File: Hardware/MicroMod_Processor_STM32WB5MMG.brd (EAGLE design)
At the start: 160 x 100 mm, 0 parts

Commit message: Nearing layout completion.
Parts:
- added C1, C2: 0.1uF, SparkFun-Capacitors:0402-TIGHT
- added D1: 120mA/40V/370mV, SparkFun-DiscreteSemi:SOD-523
- added D2: BLUE, SparkFun-LED:LED-0603
- added FD1, FD2, FD3, FD4: FIDUCIALUFIDUCIAL, SparkFun-Aesthetics:FIDUCIAL-MICRO
- added FRAME2: FRAME-LETTER, SparkFun-Aesthetics:CREATIVE_COMMONS
- added J1: MICROMOD-2222, SparkFun-MicroMod:M.2-CARD-E-22
- added LOGO1: FOUR_LAYER_WARNING, SparkFun-Aesthetics:FOUR_LAYER_WARNING
- added LOGO2: OSHW-LOGOMINI, SparkFun-Aesthetics:OSHW-LOGO-MINI
- added LOGO3: SFE_LOGO_NAME_FLAME.1_INCH, SparkFun-Aesthetics:SFE_LOGO_NAME_FLAME_.1
- added LOGO4: SPECIAL_INSTRUCTIONS-ORDERING, SparkFun-Aesthetics:ORDERING_INSTRUCTIONS
- added Q1: 20V/4.2A/52mΩ/1.4W, SparkFun-DiscreteSemi:SOT23-3
- added R1, R2: 100k, SparkFun-Resistors:0402-TIGHT
- added R3: 2.2k, SparkFun-Resistors:0402-TIGHT
- added U$1: (no value), SparkFun-MicroMod:MICROMOD_MI_LOGO_.35
- added U$2: (no value), SparkFun-MicroMod:MICROMOD_LOGO_.3
- added U$3: (no value), SparkFun-Aesthetics:SFE_LOGO_FLAME_.1
- added U1: STM32WB5MMG, stm32wb5mmg:SIP-LGA86
- added U2: W25QXX128MBIT-6X5, SparkFun-IC-Memory:WSON-8-6X5
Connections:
- new net !BOOT!: J1.11, Q1.1, R2.1
- new net !RESET!: C1.1, J1.6, U1.10
- new net 3.3V: C2.1, D1.A, J1.2, J1.74, Q1.2, R2.2, U1.17, U1.32, U1.4, U1.6, U2.8
- new net A0: J1.34, U1.8
- new net A1: J1.38, U1.7
- new net AUD_BCLK: J1.50, U1.50
- new net AUD_FSYNC: J1.52, U1.11
- new net AUD_I2S_IN: J1.54, U1.19
- new net AUD_I2S_OUT: J1.56, U1.38
- new net AUD_MCLK: J1.58, U1.14
- new net BATT_VIN: J1.49, U1.49
- new net BOOT0: Q1.3, R1.2, U1.13
- new net GND: C1.2, C2.2, D2.C, J1.1, J1.33, J1.36, J1.39, J1.45, J1.7, J1.75, J1.GND1, J1.GND2, J1.GND3, R1.1, U1.16, U1.31, U1.5, U1.57, U1.58, U1.59, U1.60, U1.84, U1.86, U2.4
- new net I2C1_INT: J1.16, U1.2
- new net I2C1_SCL: J1.14, U1.39
- new net I2C1_SDA: J1.12, U1.18
- new net I2C3_SCL: J1.53, U1.35
- new net I2C3_SDA: J1.51, U1.37
- new net LPUART_RX/DEV_TX: J1.20, U1.12
- new net LPUART_TX/DEV_RX: J1.22, U1.9
- new net N$1: D2.A, R3.1
- new net PA0/G5: J1.73, U1.3
- new net PC11/G1: J1.42, U1.23
- new net PC13/G2: J1.44, U1.40
- new net PD8/G3: J1.46, U1.75
- new net PE3/G4: J1.48, U1.72
- new net PE4/G0: J1.40, U1.42
- new net PH0/G7: J1.69, U1.61
- new net PH1/G6: J1.71, U1.62
- new net PWM0: J1.32, U1.63
- new net PWM1: J1.47, U1.76
- new net QSPI_!CS!: U1.70, U2.1
- new net QSPI_CLK: U1.56, U2.6
- new net QSPI_IO0: U1.73, U2.5
- new net QSPI_IO1: U1.80, U2.2
- new net QSPI_IO2: U1.81, U2.3
- new net QSPI_IO3: U1.67, U2.7
- new net SPI_!CS!: J1.55, U1.55
- new net SPI_PICO: J1.59, U1.52
- new net SPI_POCI: J1.61, U1.53
- new net SPI_SCK: J1.57, U1.54
- new net STAT: R3.2, U1.1
- new net SWDCK: J1.21, U1.26
- new net SWDIO: J1.23, U1.25
- new net TIM1_BKIN: J1.10, U1.41
- new net TIM1_ETR: J1.18, U1.79
- new net UART_CTS: J1.15, U1.20
- new net UART_RTS_DE: J1.13, U1.21
- new net UART_RX/DEV_TX: J1.19, U1.28
- new net UART_TX/DEV_RX: J1.17, U1.51
- new net USB_N: J1.5, U1.30
- new net USB_P: J1.3, U1.29
- new net V_BATT: D1.C, J1.72, U1.15
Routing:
- net A0: track 0.00 -> 33.5 mm, vias 0 -> 3
- net !RESET!: track 0.00 -> 31.8 mm, vias 0 -> 2
- net I2C1_INT: track 0.00 -> 31.5 mm, vias 0 -> 3
- net A1: track 0.00 -> 31.3 mm, vias 0 -> 3
- net TIM1_ETR: track 0.00 -> 27.6 mm, vias 0 -> 3
- net LPUART_TX/DEV_RX: track 0.00 -> 25.3 mm, vias 0 -> 2
- net TIM1_BKIN: track 0.00 -> 24.8 mm, vias 0 -> 2
- net PC13/G2: track 0.00 -> 24.7 mm, vias 0 -> 3
- net I2C1_SCL: track 0.00 -> 24.6 mm, vias 0 -> 2
- net LPUART_RX/DEV_TX: track 0.00 -> 24.1 mm, vias 0 -> 2
- net I2C1_SDA: track 0.00 -> 24.0 mm, vias 0 -> 1
- net AUD_I2S_OUT: track 0.00 -> 23.6 mm, vias 0 -> 2
- net QSPI_CLK: track 0.00 -> 23.4 mm, vias 0 -> 2
- net PD8/G3: track 0.00 -> 23.3 mm, vias 0 -> 4
- net QSPI_IO3: track 0.00 -> 22.9 mm, vias 0 -> 2
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- added copper zone on layer 15, net 3.3V
- added copper zone on layer 1, net GND
- added copper zone on layer 16, net GND
- added copper zone on layer 2, net GND
- added copper zone on layer 15, net GND1
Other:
- board size 160 x 100 mm -> 22 x 22 mm
- board text added: "Alex Brudner"

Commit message: Layout complete.
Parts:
- added TP1, TP2, TP3, TP4, TP5, TP6, TP7, TP8: TEST-POINT3, SparkFun-Connectors:PAD.03X.03
- added U$4, U$5: (no value), output:STM32WB5MMG0
- added U$6: (no value), SparkFun-Aesthetics:SFE_LOGO_FLAME_STOP_.1
- moved U$3 49.4 mm to (10.8, 12.6)
- moved U$2 47.7 mm to (14.6, 10.2), flipped to the bottom, turned to 90 degrees
- moved U$1 47.1 mm to (17.9, 7.15)
- moved LOGO3 34.3 mm to (18.1, 10.6), flipped to the bottom, turned to 90 degrees
- moved LOGO2 31.6 mm to (16.0, 17.0)
- moved FRAME2 21.2 mm to (52.1, -18.6)
- moved LOGO1 21.2 mm to (28.4, 30.4)
- moved LOGO4 21.2 mm to (25.7, 42.5)
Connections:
- net BOOT0: now also TP1.1
- net QSPI_!CS!: now also TP4.1
- net QSPI_CLK: now also TP3.1
- net QSPI_IO0: now also TP5.1
- net QSPI_IO1: now also TP6.1
- net QSPI_IO2: now also TP7.1
- net QSPI_IO3: now also TP8.1
- net STAT: now also TP2.1
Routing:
- net PH0/G7: track 0.00 -> 26.1 mm, vias 1 -> 3
- net PH1/G6: track 0.00 -> 25.5 mm, vias 1 -> 3
- net QSPI_IO2: track 10.2 -> 14.0 mm
- net STAT: track 18.2 -> 20.3 mm
- net PD8/G3: track 23.3 -> 25.3 mm
- net QSPI_!CS!: track 8.92 -> 10.7 mm
- net GND: track 1.32 -> 0.00 mm, vias 35 -> 41
- net QSPI_IO1: track 11.2 -> 12.1 mm
- net QSPI_IO3: track 22.9 -> 23.8 mm
- net BOOT0: track 16.2 -> 17.0 mm
- net AUD_MCLK: track 14.9 -> 15.6 mm
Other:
- board text added: "1"
- board text added: "2"
- board text added: "3"
- board text added: "4"
- board text added: "Beveled Edge"
- board text added: "Board Thickness is 0.8mm"
- board text added: "ENIG Finish"
- board text added: "v01"

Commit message: Last update for protos.
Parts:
- added U$7: (no value), output:STAT0
- moved TP3 13.3 mm to (5.08, 15.2)
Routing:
- net QSPI_CLK: track 23.7 -> 22.7 mm
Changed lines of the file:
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@@
 <layer number="29" name="tStop" color="7" fill="3" visible="yes" active="yes"/>
 <layer number="30" name="bStop" color="7" fill="6" visible="yes" active="yes"/>
-<layer number="31" name="tCream" color="7" fill="4" visible="no" active="yes"/>
+<layer number="31" name="tCream" color="7" fill="4" visible="yes" active="yes"/>
 <layer number="32" name="bCream" color="7" fill="5" visible="no" active="yes"/>
 <layer number="33" name="tFinish" color="6" fill="3" visible="no" active="yes"/>
@@
 <elements>
 <element name="J1" library="SparkFun-MicroMod" package="M.2-CARD-E-22" value="MICROMOD-2222" x="11" y="0" smashed="yes"/>
-<element name="U1" library="stm32wb5mmg" package="SIP-LGA86" value="STM32WB5MMG" x="4.95" y="16.1" locked="yes" smashed="yes">
-<attribute name="PROD_ID" value="IC-17415" x="4.92" y="16.13" locked="yes" size="1.778" layer="27" display="off"/>
+<element name="U1" library="stm32wb5mmg" package="SIP-LGA86" value="STM32WB5MMG" x="4.95" y="16.1" smashed="yes">
+<attribute name="PROD_ID" value="IC-17415" x="4.92" y="16.13" size="1.778" layer="27" display="off"/>
 </element>
 <element name="C1" library="SparkFun-Capacitors" package="0402-TIGHT" value="0.1uF" x="1.55" y="7.7" smashed="yes">
@@
 <element name="U$5" library="output" package="STM32WB5MMG0" value="" x="16.1" y="10.7" smashed="yes" rot="MR90"/>
 <element name="U$6" library="SparkFun-Aesthetics" package="SFE_LOGO_FLAME_STOP_.1" value="" x="19.25" y="19.8" smashed="yes" rot="MR0"/>
-<element name="TP3" library="SparkFun-Connectors" package="PAD.03X.03" value="TEST-POINT3" x="17.78" y="11.43" smashed="yes" rot="MR0"/>
+<element name="TP3" library="SparkFun-Connectors" package="PAD.03X.03" value="TEST-POINT3" x="5.08" y="15.24" smashed="yes" rot="MR0"/>
 <element name="TP4" library="SparkFun-Connectors" package="PAD.03X.03" value="TEST-POINT3" x="13.97" y="11.43" smashed="yes" rot="MR0"/>
 <element name="TP5" library="SparkFun-Connectors" package="PAD.03X.03" value="TEST-POINT3" x="20.32" y="11.43" smashed="yes" rot="MR0"/>
@@
 <element name="TP1" library="SparkFun-Connectors" package="PAD.03X.03" value="TEST-POINT3" x="11.43" y="10.16" smashed="yes" rot="MR0"/>
 <element name="TP2" library="SparkFun-Connectors" package="PAD.03X.03" value="TEST-POINT3" x="20.32" y="16.51" smashed="yes" rot="MR0"/>
+<element name="U$7" library="output" package="STAT0" value="" x="19.8" y="18.4" smashed="yes"/>
 </elements>
 <signals>
@@
 <wire x1="17.8" y1="12.4" x2="12.25" y2="12.4" width="0.15" layer="16"/>
 <wire x1="12.1" y1="12.25" x2="12.25" y2="12.4" width="0.15" layer="16"/>
-<wire x1="19.45" y1="10.75" x2="18.3" y2="11.9" width="0.15" layer="16"/>
-<wire x1="18.3" y1="11.9" x2="17.8" y2="12.4" width="0.15" layer="16"/>
+<wire x1="19.45" y1="10.75" x2="17.8" y2="12.4" width="0.15" layer="16"/>
 <wire x1="7.75" y1="12.25" x2="12.1" y2="12.25" width="0.15" layer="16"/>
 <wire x1="7.75" y1="12.25" x2="6.8" y2="13.2" width="0.15" layer="16"/>
-<wire x1="6.8" y1="13.2" x2="6.8" y2="13.4" width="0.15" layer="16"/>
-<wire x1="6.8" y1="13.4" x2="6.55" y2="13.65" width="0.15" layer="16"/>
-<wire x1="6.55" y1="13.65" x2="6.15" y2="13.65" width="0.15" layer="16"/>
-<wire x1="6.15" y1="13.65" x2="4.05" y2="15.75" width="0.15" layer="16"/>
-<wire x1="4.05" y1="17.65" x2="4.05" y2="15.75" width="0.15" layer="16"/>
-<wire x1="4.05" y1="17.65" x2="4" y2="17.7" width="0.15" layer="16"/>
 <contactref element="TP3" pad="1"/>
-<wire x1="17.78" y1="11.43" x2="17.83" y2="11.43" width="0.15" layer="16"/>
-<wire x1="17.83" y1="11.43" x2="18.3" y2="11.9" width="0.15" layer="16"/>
+<wire x1="6.8" y1="13.52" x2="5.08" y2="15.24" width="0.15" layer="16"/>
+<wire x1="6.8" y1="13.2" x2="6.8" y2="13.52" width="0.15" layer="16"/>
+<wire x1="4.0036" y1="16.96718125" x2="4" y2="16.97078125" width="0.15" layer="16"/>
+<wire x1="4" y1="16.97078125" x2="4" y2="17.7" width="0.15" layer="16"/>
+<wire x1="5.08" y1="15.24" x2="4.0036" y2="16.3164" width="0.15" layer="16"/>
+<wire x1="4.0036" y1="16.3164" x2="4.0036" y2="16.96718125" width="0.15" layer="16"/>
 </signal>
 <signal name="QSPI_!CS!">

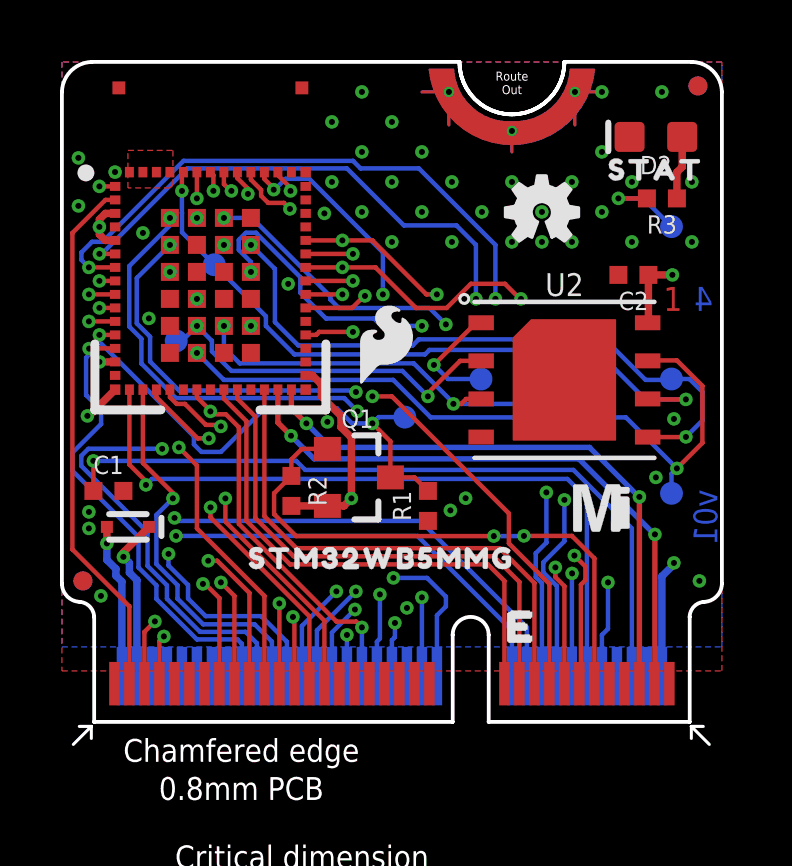
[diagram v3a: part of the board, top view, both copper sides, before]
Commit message: Updates from Design Review v01
Fix footprint.
Reposition bottom silk
Removed extraneous vias.
Renamed some nets to match micromod connector.
Rerouted some traces.
Added ground vias near fast switching vias.
Moved traces to expand ground plane.
Removed all but BOOT0 test point with Chris' approval.
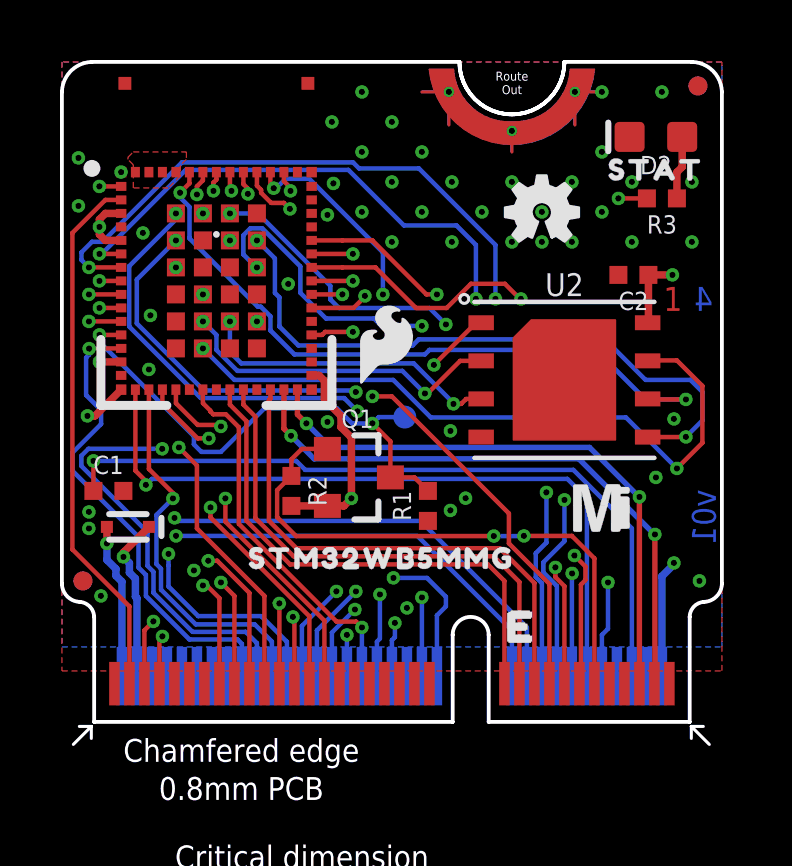
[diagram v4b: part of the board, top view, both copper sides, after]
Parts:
- removed TP2, TP3, TP4, TP5, TP6, TP7, TP8: TEST-POINT3, SparkFun-Connectors:PAD.03X.03
- moved U$5 15.1 mm to (4.85, 20.8), turned to 0 degrees
- moved LOGO3 2.89 mm to (15.6, 11.9), turned to 0 degrees
- moved U$2 1.28 mm to (15.6, 9.35), turned to 0 degrees
- moved U1 0.25 mm to (5.15, 16.2)
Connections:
- net I2C3_SCL renamed I2C3_SCL1
- net I2C3_SDA renamed I2C3_SDA1
- net LPUART_RX/DEV_TX renamed LP_RX2/DEV_TX2
- net LPUART_TX/DEV_RX renamed LP_TX2/DEV_RX2
- net UART_RX/DEV_TX renamed RX1/DEV_TX1
- net UART_TX/DEV_RX renamed TX1/DEV_RX1
- net QSPI_!CS!: no longer TP4.1
- net QSPI_CLK: no longer TP3.1
- net QSPI_IO0: no longer TP5.1
- net QSPI_IO1: no longer TP6.1
- net QSPI_IO2: no longer TP7.1
- net QSPI_IO3: no longer TP8.1
- net STAT: no longer TP2.1
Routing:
- net QSPI_IO2: track 14.0 -> 10.2 mm
- net STAT: track 20.3 -> 18.0 mm
- net QSPI_!CS!: track 10.7 -> 8.78 mm
- net QSPI_IO1: track 12.1 -> 11.0 mm
- net QSPI_IO3: track 23.8 -> 22.7 mm
- net 3.3V: track 21.5 -> 22.1 mm
- net PE4/G0: track 20.4 -> 20.2 mm, vias 3 -> 2
- net PC13/G2: track 24.9 -> 24.7 mm, vias 3 -> 2
- net PC11/G1: track 12.5 -> 12.4 mm, vias 2 -> 1

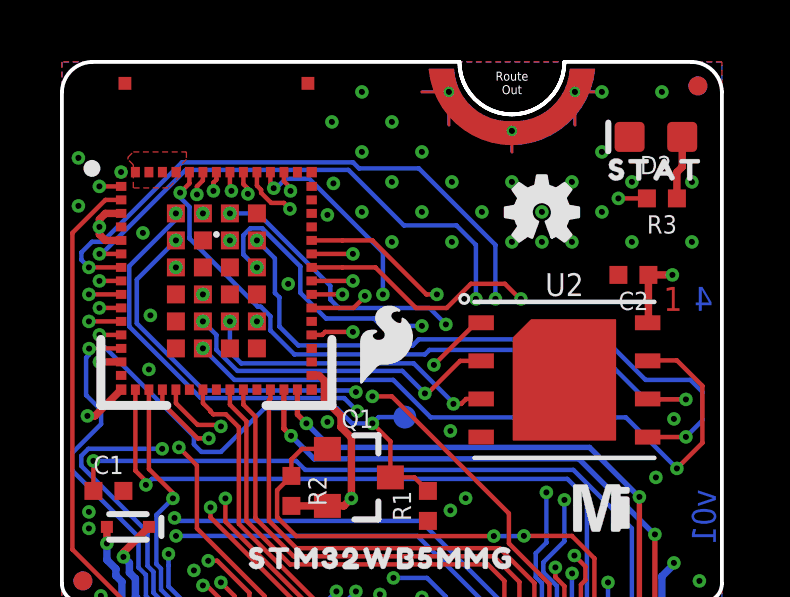
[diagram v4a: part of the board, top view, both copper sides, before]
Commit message: Protos commit
Schematic - Revector all fonts
Board - Straighten one trace.
Panel - Panelize and CAM.
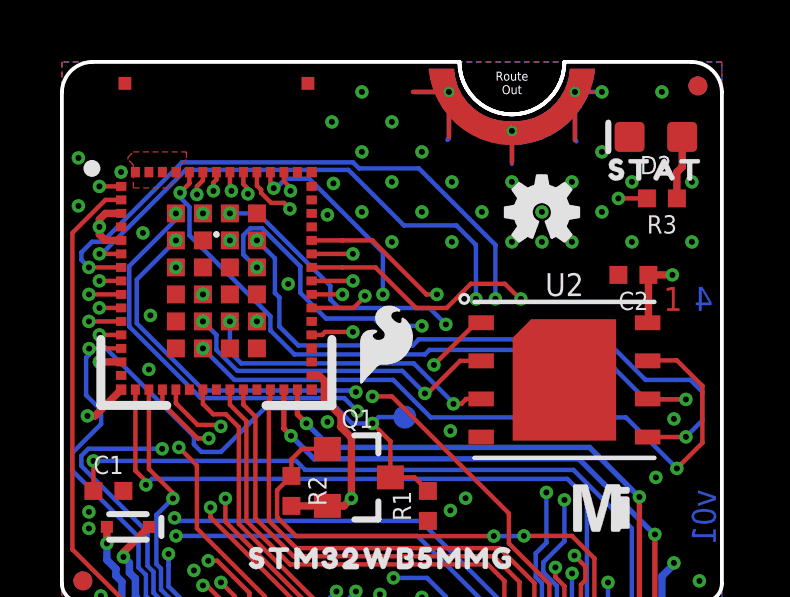
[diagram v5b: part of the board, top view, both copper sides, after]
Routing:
- net GND: track 0.00 -> 11.8 mm
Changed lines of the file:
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@@
 <via x="12.95" y="9.7" extent="1-16" drill="0.2"/>
 <via x="2.9" y="11.75" extent="1-16" drill="0.2"/>
+<wire x1="12.9" y1="21" x2="12.9" y2="19.5" width="0.15" layer="1"/>
+<wire x1="12.9" y1="21" x2="11.7" y2="21" width="0.15" layer="1"/>
+<wire x1="15" y1="19.7" x2="15" y2="18.65" width="0.15" layer="1"/>
+<wire x1="17.1" y1="21" x2="17.1" y2="19.4" width="0.15" layer="1"/>
+<wire x1="15" y1="19.7" x2="15" y2="18.6" width="0.15" layer="16"/>
+<wire x1="17.1" y1="19.4" x2="17.15" y2="19.35" width="0.15" layer="16"/>
+<wire x1="12.9" y1="21" x2="11.75" y2="21" width="0.15" layer="16"/>
+<wire x1="12.9" y1="21" x2="12.9" y2="19.45" width="0.15" layer="16"/>
+<wire x1="12.9" y1="19.45" x2="12.85" y2="19.4" width="0.15" layer="16"/>
+<wire x1="17.1" y1="21" x2="17.1" y2="19.4" width="0.15" layer="16"/>
+<wire x1="17.1" y1="21" x2="18" y2="21" width="0.15" layer="16"/>
 </signal>
 <signal name="!RESET!">
@@
 <wire x1="7.75" y1="12.25" x2="12.1" y2="12.25" width="0.15" layer="16"/>
 <wire x1="7.75" y1="12.25" x2="6.95" y2="13.05" width="0.15" layer="16"/>
-<wire x1="6.95" y1="13.52" x2="6.63" y2="13.84" width="0.15" layer="16"/>
-<wire x1="6.63" y1="13.84" x2="6.53" y2="13.84" width="0.15" layer="16"/>
 <wire x1="6.95" y1="13.05" x2="6.95" y2="13.52" width="0.15" layer="16"/>
 <wire x1="4.2536" y1="17.16718125" x2="3.94" y2="17.48078125" width="0.15" layer="16"/>
 <wire x1="3.94" y1="17.48078125" x2="3.94" y2="17.64" width="0.15" layer="16"/>
-<wire x1="4.2536" y1="16.15" x2="4.2536" y2="17.16718125" width="0.15" layer="16"/>
+<wire x1="4.2536" y1="16.2164" x2="4.2536" y2="17.16718125" width="0.15" layer="16"/>
 <wire x1="3.94" y1="17.64" x2="4.25" y2="17.95" width="0.15" layer="1"/>
 <wire x1="4.25" y1="17.95" x2="4.25" y2="18.325" width="0.15" layer="1"/>
-<wire x1="4.2536" y1="16.1164" x2="4.2536" y2="16.15" width="0.15" layer="16"/>
-<wire x1="6.53" y1="13.84" x2="4.2536" y2="16.1164" width="0.15" layer="16"/>
+<wire x1="6.95" y1="13.52" x2="4.2536" y2="16.2164" width="0.15" layer="16"/>
 </signal>
 <signal name="QSPI_!CS!">
@@
 <signal name="PC11/G1">
 <contactref element="U1" pad="23"/>
-<wire x1="4.95" y1="10.35" x2="4.95" y2="10.375" width="0.15" layer="1"/>
-<wire x1="4.95" y1="10.375" x2="4.7" y2="10.625" width="0.15" layer="1"/>
-<wire x1="4.7" y1="11.075" x2="4.7" y2="10.625" width="0.15" layer="1"/>
+<wire x1="5.0464" y1="10.2536" x2="4.7" y2="10.6" width="0.15" layer="1"/>
+<wire x1="4.7" y1="11.075" x2="4.7" y2="10.6" width="0.15" layer="1"/>
 <contactref element="J1" pad="42"/>
-<wire x1="4.95" y1="10.35" x2="5.0464" y2="10.2536" width="0.15" layer="1"/>
 <wire x1="5.0464" y1="10.2536" x2="5.46718125" y2="10.2536" width="0.15" layer="1"/>
 <wire x1="5.46718125" y1="10.2536" x2="5.8984" y2="9.82238125" width="0.15" layer="1"/>
@@
 <polygon width="0.1" layer="15" pour="cutout">
 <vertex x="7.9" y="22"/>
-<vertex x="7.9" y="19.15"/>
-<vertex x="0" y="19.15"/>
+<vertex x="7.9" y="19.2"/>
+<vertex x="0" y="19.2"/>
 <vertex x="0" y="22"/>
 </polygon>
